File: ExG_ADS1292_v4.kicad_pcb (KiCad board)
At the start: 2 copper layers, 32.2 x 20.5 mm, 67 parts, among them P1 CONN_2, P2 CONN_2, P3 CONN_2, P4 CONN_1, P5 CONN_01X04, Q1 DMP21D5UFB4-7B, U1 TPS63001, U2 ADS1291/2, U3 NRF528XX-QFAA, U4 MPU-9250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

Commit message: Replace pin header holes with pads.
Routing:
- net DGND: vias 11 -> 12

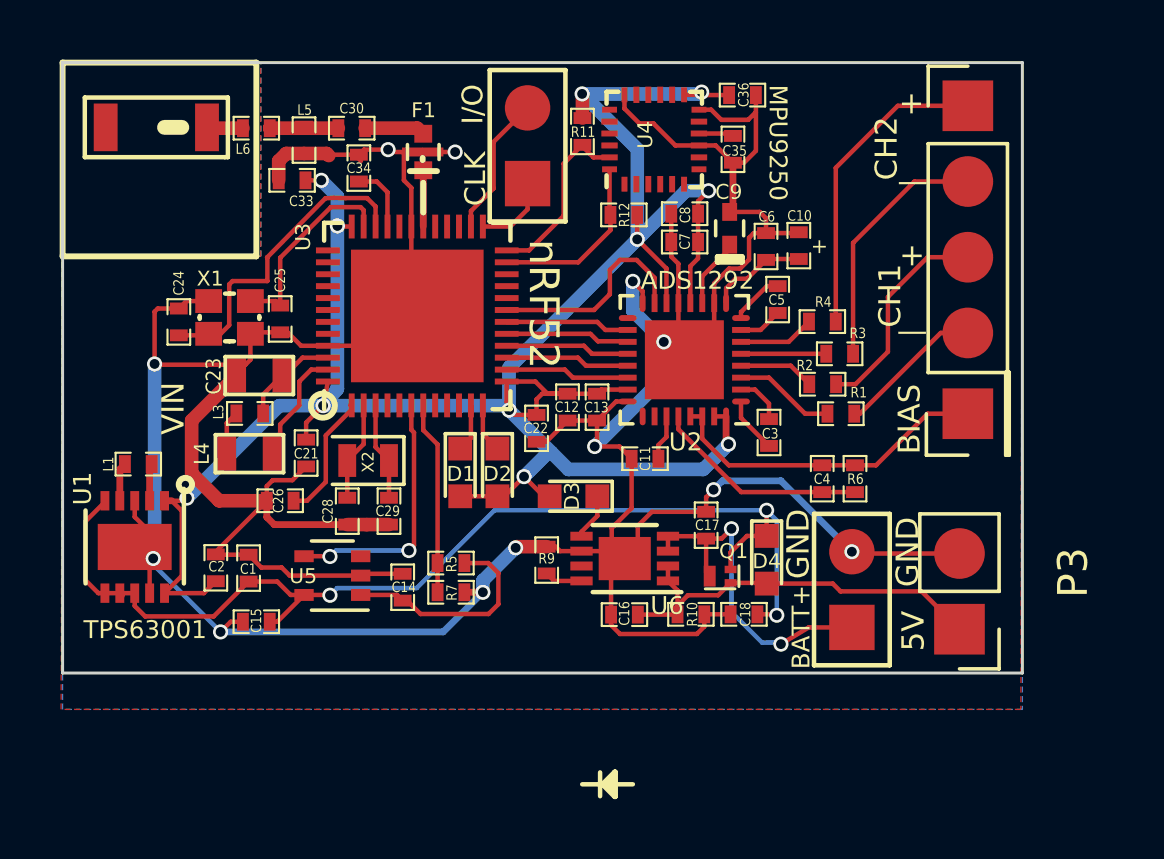
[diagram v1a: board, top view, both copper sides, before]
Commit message: Added SSAJ switch, fixed annotations.
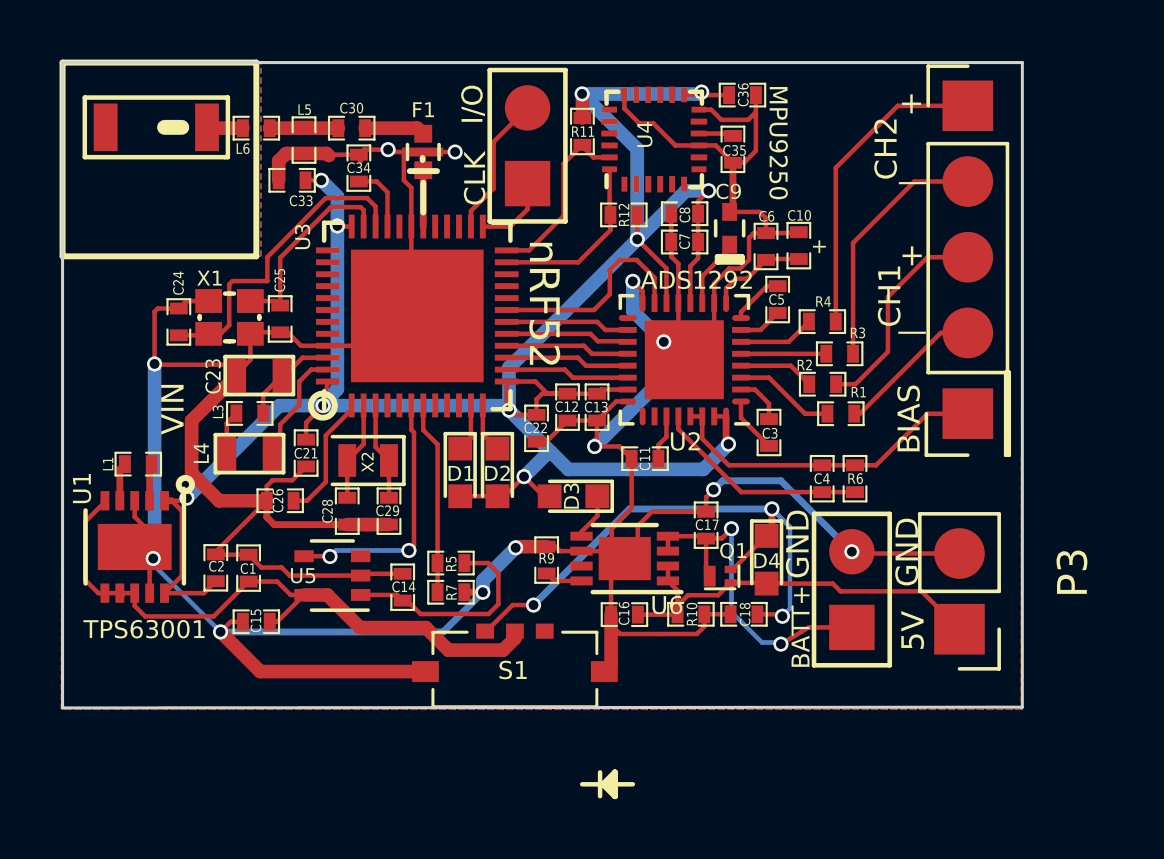
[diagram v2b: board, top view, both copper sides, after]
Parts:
- added S1: SSAJ120100, SSAJ120100, F.Cu at (280.1, 144.6)
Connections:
- C18 pad 2: VCC -> VccSwitch
- D4 pad 1: VCC -> VccSwitch
- Q1 pad 3: VCC -> VccSwitch
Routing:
- net VccSwitch: track 0.00 -> 18.8 mm, vias 0 -> 3
- net VCC: track 37.3 -> 21.6 mm, vias 3 -> 0
- net DGND: track 163.8 -> 173.3 mm
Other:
- board size 32.2 x 20.5 mm -> 32.2 x 21.7 mm
